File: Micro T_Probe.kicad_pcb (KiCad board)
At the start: 2 copper layers, 6.4 x 14 mm, 11 parts, among them P1 CONN_5, P2 CONN_5, U1 TMP_102

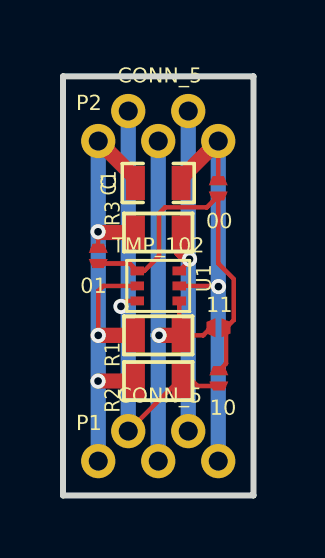
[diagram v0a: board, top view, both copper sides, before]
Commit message: Updated the solderability of this board by removing the mask above the solder junctions and enlarging the pads.
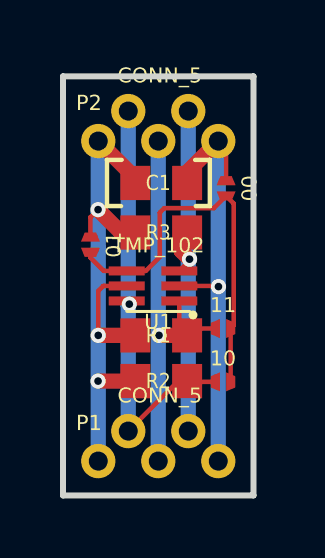
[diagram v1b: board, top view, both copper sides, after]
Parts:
- C1: footprint SM0603_Capa -> SM0603_CAPAHAND
- GS1: renamed from 00; value GS2 -> 00
- GS2: renamed from 01; value GS2 -> 01
- GS3: renamed from 11; value GS2 -> 11
- GS4: renamed from 10; value GS2 -> 10
- R1, R2, R3: footprint SM0603 -> SM0603_HAND
- moved GS2 0.46 mm to (26.3, 31.0)
- moved GS1 0.26 mm to (30.8, 29.1)
- moved GS4 0.18 mm to (30.7, 35.6), turned to 180 degrees
- moved GS3 0.15 mm to (30.7, 33.8)
- turned R1 to 0 degrees
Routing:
- net /VCC: track 20.4 -> 21.9 mm
- net /SDA: track 15.8 -> 14.7 mm
- net /ADD: track 12.2 -> 13.1 mm
